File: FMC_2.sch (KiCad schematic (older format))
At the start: 14 parts, among them P2 SAMTEC_ASP-134603-01

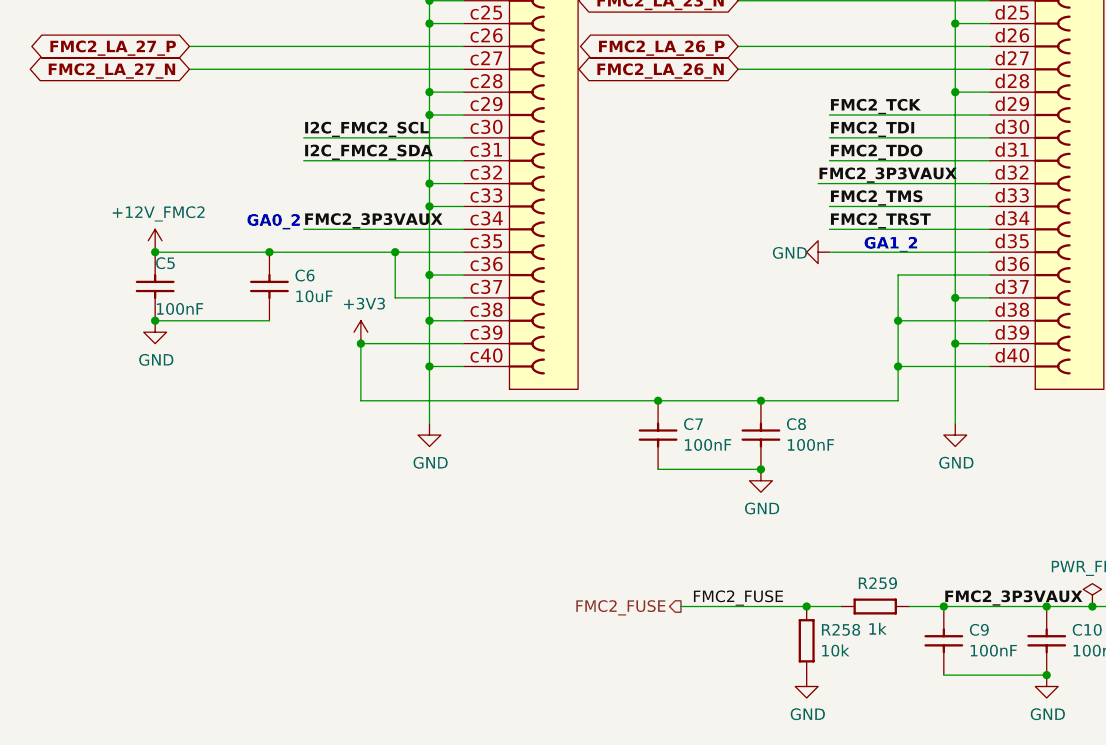
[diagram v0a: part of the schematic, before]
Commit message: Add 300 Ohm series resistors to GA pins
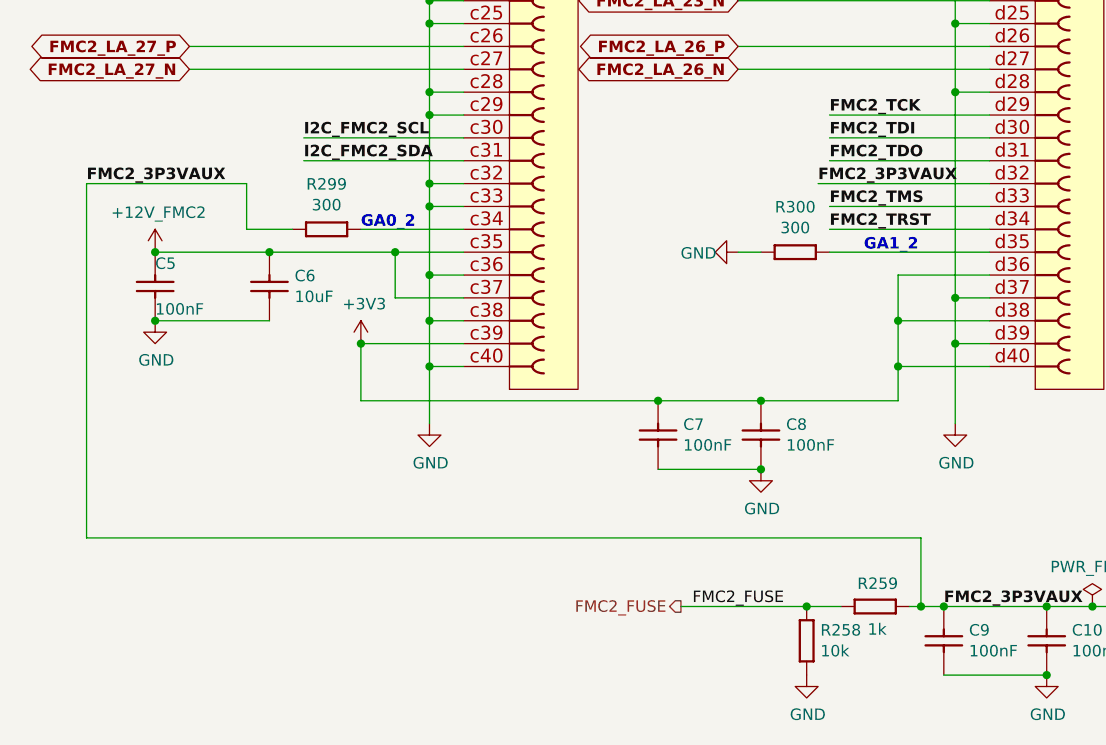
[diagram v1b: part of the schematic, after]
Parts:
- added R299, R300: R0402_300R_1%_0.0625W_100PPM, Resistors SMD:RESC1005X40N, symbol Resistors_SMD:R0402_300R_1%_0.0625W_100PPM
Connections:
- net FMC2_3P3VAUX: now also R299.1; no longer P2.c34
- net GND: now also R300.1; no longer P2.d35
- new net: P2.c34, R299.2
- new net: P2.d35, R300.2
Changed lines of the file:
@@
 Connection ~ 5750 5850
-Wire Wire Line
-	3150 5250 3850 5250
 Wire Wire Line
 	3150 4850 3850 4850
@@
 Wire Wire Line
 	5450 5150 6150 5150
-Wire Wire Line
-	5450 5350 6150 5350
 Text Label 8000 2050 0    50   ~ 10
 FMC2_CLK1_M2C_P
@@
 Wire Wire Line
 	5450 5250 6150 5250
-Text Label 3150 5250 0    50   ~ 10
+Text Label 2200 5050 0    50   ~ 10
 FMC2_3P3VAUX
-Text Notes 2900 5250 0    50   ~ 10
+Text Notes 3400 5250 0    50   ~ 10
 GA0_2
 $Comp
 L power:GND #PWR?
 U 1 1 5D1DC9A3
-P 5450 5350
+P 5050 5350
 AR Path="/5BD32060/5D1DC9A3" Ref="#PWR?"  Part="1"
 AR Path="/5BD31F9A/5D1DC9A3" Ref="#PWR?"  Part="1"
 AR Path="/5BD31F9F/5D1DC9A3" Ref="#PWR0101"  Part="1"
 AR Path="/5D1DC9A3" Ref="#PWR?"  Part="1"
-F 0 "#PWR0101" H 5450 5100 50  0001 C CNN
-F 1 "GND" V 5455 5177 50  0000 C CNN
-F 2 "" H 5450 5350 50  0001 C CNN
-F 3 "" H 5450 5350 50  0001 C CNN
-	1    5450 5350
+F 0 "#PWR0101" H 5050 5100 50  0001 C CNN
+F 1 "GND" V 5055 5177 50  0000 C CNN
+F 2 "" H 5050 5350 50  0001 C CNN
+F 3 "" H 5050 5350 50  0001 C CNN
+	1    5050 5350
 	0    1    1    0
 $EndComp
@@
 $EndComp
 Wire Wire Line
-	5800 6900 5950 6900
+	5800 6900 5850 6900
 Connection ~ 5950 6900
 Wire Wire Line
@@
 Wire Wire Line
 	7150 6900 7300 6900
+$Comp
+L Resistors_SMD:R0402_300R_1%_0.0625W_100PPM R299
+U 1 1 5ED979B2
+P 3100 5250
+F 0 "R299" H 3250 5447 50  0000 C CNN
+F 1 "R0402_300R_1%_0.0625W_100PPM" H 3100 5055 50  0001 L CNN
+F 2 "Resistors SMD:RESC1005X40N" H 3100 4980 50  0001 L CNN
+F 3 " " H 3100 4905 50  0001 L CNN
+F 4 "300" H 3250 5356 50  0000 C CNN "Val"
+F 5 "R0402_300R_1%_0.0625W_100PPM" H 3100 4830 50  0001 L CNN "Part Number"
+F 6 "Resistor - 1%" H 3100 4755 50  0001 L CNN "Library Ref"
+F 7 "SchLib\\Resistors.SchLib" H 3100 4680 50  0001 L CNN "Library Path"
+F 8 "300" H 3100 4605 50  0001 L CNN "Comment"
+F 9 "Standard" H 3100 4530 50  0001 L CNN "Component Kind"
+F 10 "Standard" H 3100 4455 50  0001 L CNN "Component Type"
+F 11 " " H 3100 4380 50  0001 L CNN "PackageDescription"
+F 12 "2" H 3100 4305 50  0001 L CNN "Pin Count"
+F 13 "PcbLib\\Resistors SMD.PcbLib" H 3100 4230 50  0001 L CNN "Footprint Path"
+F 14 "RESC1005X40N" H 3100 4155 50  0001 L CNN "Footprint Ref"
+F 15 "Not Recommended" H 3100 4080 50  0001 L CNN "Status"
+F 16 "0.0625W" H 3100 4005 50  0001 L CNN "Power"
+F 17 "±100ppm/°C" H 3100 3930 50  0001 L CNN "TC"
+F 18 " " H 3100 3855 50  0001 L CNN "Voltage"
+F 19 "±1%" H 3100 3780 50  0001 L CNN "Tolerance"
+F 20 "General Purpose Thick Film Chip Resistor" H 3100 3705 50  0001 L CNN "Part Description"
+F 21 "GENERIC" H 3100 3630 50  0001 L CNN "Manufacturer"
+F 22 "R0402_300R_1%_0.0625W_100PPM" H 3100 3555 50  0001 L CNN "Manufacturer Part Number"
+F 23 "0402" H 3100 3480 50  0001 L CNN "Case"
+F 24 "No" H 3100 3405 50  0001 L CNN "PressFit"
+F 25 "Yes" H 3100 3330 50  0001 L CNN "Mounted"
+F 26 " " H 3100 3255 50  0001 L CNN "Sense Comment"
+F 27 "No" H 3100 3180 50  0001 L CNN "Sense"
+F 28 " " H 3100 3105 50  0001 L CNN "Status Comment"
+F 29 "No" H 3100 3030 50  0001 L CNN "Socket"
+F 30 "Yes" H 3100 2955 50  0001 L CNN "SMD"
+F 31 " " H 3100 2880 50  0001 L CNN "ComponentHeight"
+F 32 "YAGEO PHYCOMP" H 3100 2805 50  0001 L CNN "Manufacturer1 Example"
+F 33 "232270673001L" H 3100 2730 50  0001 L CNN "Manufacturer1 Part Number"
+F 34 "0.4mm" H 3100 2655 50  0001 L CNN "Manufacturer1 ComponentHeight"
+F 35 "CERN DEM JLC" H 3100 2580 50  0001 L CNN "Author"
+F 36 "12/03/07 00:00:00" H 3100 2505 50  0001 L CNN "CreateDate"
+F 37 "10/17/12 00:00:00" H 3100 2430 50  0001 L CNN "LatestRevisionDate"
+F 38 "Resistors SMD" H 3100 2355 50  0001 L CNN "Database Table Name"
+F 39 "Resistors.DbLib" H 3100 2280 50  0001 L CNN "Library Name"
+F 40 "Resistors SMD" H 3100 2205 50  0001 L CNN "Footprint Library"
+F 41 "This work is licensed under the Creative Commons CC-BY-SA 4.0 License. To the extent that circuit schematics that use Licensed Material can be considered to be ‘Adapted Material’, then the copyright holder waives article 3.b of the license with respect to these schematics." H 3100 2130 50  0001 L CNN "License"
+	1    3100 5250
+	1    0    0    -1
+$EndComp
+Wire Wire Line
+	3850 5250 3400 5250
+$Comp
+L Resistors_SMD:R0402_300R_1%_0.0625W_100PPM R300
+U 1 1 5EDF3EEE
+P 5150 5350
+F 0 "R300" H 5300 5547 50  0000 C CNN
+F 1 "R0402_300R_1%_0.0625W_100PPM" H 5150 5155 50  0001 L CNN
+F 2 "Resistors SMD:RESC1005X40N" H 5150 5080 50  0001 L CNN
+F 3 " " H 5150 5005 50  0001 L CNN
+F 4 "300" H 5300 5456 50  0000 C CNN "Val"
+F 5 "R0402_300R_1%_0.0625W_100PPM" H 5150 4930 50  0001 L CNN "Part Number"
+F 6 "Resistor - 1%" H 5150 4855 50  0001 L CNN "Library Ref"
+F 7 "SchLib\\Resistors.SchLib" H 5150 4780 50  0001 L CNN "Library Path"
+F 8 "300" H 5150 4705 50  0001 L CNN "Comment"
+F 9 "Standard" H 5150 4630 50  0001 L CNN "Component Kind"
+F 10 "Standard" H 5150 4555 50  0001 L CNN "Component Type"
+F 11 " " H 5150 4480 50  0001 L CNN "PackageDescription"
+F 12 "2" H 5150 4405 50  0001 L CNN "Pin Count"
+F 13 "PcbLib\\Resistors SMD.PcbLib" H 5150 4330 50  0001 L CNN "Footprint Path"
+F 14 "RESC1005X40N" H 5150 4255 50  0001 L CNN "Footprint Ref"
+F 15 "Not Recommended" H 5150 4180 50  0001 L CNN "Status"
+F 16 "0.0625W" H 5150 4105 50  0001 L CNN "Power"
+F 17 "±100ppm/°C" H 5150 4030 50  0001 L CNN "TC"
+F 18 " " H 5150 3955 50  0001 L CNN "Voltage"
+F 19 "±1%" H 5150 3880 50  0001 L CNN "Tolerance"
+F 20 "General Purpose Thick Film Chip Resistor" H 5150 3805 50  0001 L CNN "Part Description"
+F 21 "GENERIC" H 5150 3730 50  0001 L CNN "Manufacturer"
+F 22 "R0402_300R_1%_0.0625W_100PPM" H 5150 3655 50  0001 L CNN "Manufacturer Part Number"
+F 23 "0402" H 5150 3580 50  0001 L CNN "Case"
+F 24 "No" H 5150 3505 50  0001 L CNN "PressFit"
+F 25 "Yes" H 5150 3430 50  0001 L CNN "Mounted"
+F 26 " " H 5150 3355 50  0001 L CNN "Sense Comment"
+F 27 "No" H 5150 3280 50  0001 L CNN "Sense"
+F 28 " " H 5150 3205 50  0001 L CNN "Status Comment"
+F 29 "No" H 5150 3130 50  0001 L CNN "Socket"
+F 30 "Yes" H 5150 3055 50  0001 L CNN "SMD"
+F 31 " " H 5150 2980 50  0001 L CNN "ComponentHeight"
+F 32 "YAGEO PHYCOMP" H 5150 2905 50  0001 L CNN "Manufacturer1 Example"
+F 33 "232270673001L" H 5150 2830 50  0001 L CNN "Manufacturer1 Part Number"
+F 34 "0.4mm" H 5150 2755 50  0001 L CNN "Manufacturer1 ComponentHeight"
+F 35 "CERN DEM JLC" H 5150 2680 50  0001 L CNN "Author"
+F 36 "12/03/07 00:00:00" H 5150 2605 50  0001 L CNN "CreateDate"
+F 37 "10/17/12 00:00:00" H 5150 2530 50  0001 L CNN "LatestRevisionDate"
+F 38 "Resistors SMD" H 5150 2455 50  0001 L CNN "Database Table Name"
+F 39 "Resistors.DbLib" H 5150 2380 50  0001 L CNN "Library Name"
+F 40 "Resistors SMD" H 5150 2305 50  0001 L CNN "Footprint Library"
+F 41 "This work is licensed under the Creative Commons CC-BY-SA 4.0 License. To the extent that circuit schematics that use Licensed Material can be considered to be ‘Adapted Material’, then the copyright holder waives article 3.b of the license with respect to these schematics." H 5150 2230 50  0001 L CNN "License"
+	1    5150 5350
+	1    0    0    -1
+$EndComp
+Wire Wire Line
+	5150 5350 5050 5350
+Wire Wire Line
+	5450 5350 6150 5350
+Wire Wire Line
+	3100 5250 2900 5250
+Wire Wire Line
+	2900 5250 2900 5050
+Wire Wire Line
+	2900 5050 2200 5050
+Wire Wire Line
+	5850 6900 5850 6600
+Wire Wire Line
+	5850 6600 2200 6600
+Wire Wire Line
+	2200 6600 2200 5050
+Connection ~ 5850 6900
+Wire Wire Line
+	5850 6900 5950 6900
 $EndSCHEMATC

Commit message: change R297 - R300 to 240 Ohm
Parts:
- R299, R300: value R0402_300R_1%_0.0625W_100PPM -> R0402_240R_1%_0.0625W_100PPM; footprint Resistors SMD:RESC1005X40N -> Marble:RESC1005X40N; symbol Resistors_SMD:R0402_300R_1%_0.0625W_100PPM -> Resistors_SMD:R0402_240R_1%_0.0625W_100PPM; Comment 300 -> 240; Manufacturer Part Number R0402_300R_1%_0.0625W_100PPM -> R0402_240R_1%_0.0625W_100PPM; Manufacturer1 Part Number 232270673001L -> 232270672401L; Part Number R0402_300R_1%_0.0625W_100PPM -> R0402_240R_1%_0.0625W_100PPM; Val 300 -> 240
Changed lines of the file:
@@
 	7150 6900 7300 6900
 $Comp
-L Resistors_SMD:R0402_300R_1%_0.0625W_100PPM R299
+L Resistors_SMD:R0402_240R_1%_0.0625W_100PPM R299
 U 1 1 5ED979B2
 P 3100 5250
 F 0 "R299" H 3250 5447 50  0000 C CNN
-F 1 "R0402_300R_1%_0.0625W_100PPM" H 3100 5055 50  0001 L CNN
-F 2 "Resistors SMD:RESC1005X40N" H 3100 4980 50  0001 L CNN
+F 1 "R0402_240R_1%_0.0625W_100PPM" H 3100 5055 50  0001 L CNN
+F 2 "Marble:RESC1005X40N" H 3100 4980 50  0001 L CNN
 F 3 " " H 3100 4905 50  0001 L CNN
-F 4 "300" H 3250 5356 50  0000 C CNN "Val"
-F 5 "R0402_300R_1%_0.0625W_100PPM" H 3100 4830 50  0001 L CNN "Part Number"
+F 4 "240" H 3250 5356 50  0000 C CNN "Val"
+F 5 "R0402_240R_1%_0.0625W_100PPM" H 3100 4830 50  0001 L CNN "Part Number"
 F 6 "Resistor - 1%" H 3100 4755 50  0001 L CNN "Library Ref"
 F 7 "SchLib\\Resistors.SchLib" H 3100 4680 50  0001 L CNN "Library Path"
-F 8 "300" H 3100 4605 50  0001 L CNN "Comment"
+F 8 "240" H 3100 4605 50  0001 L CNN "Comment"
 F 9 "Standard" H 3100 4530 50  0001 L CNN "Component Kind"
 F 10 "Standard" H 3100 4455 50  0001 L CNN "Component Type"
@@
 F 20 "General Purpose Thick Film Chip Resistor" H 3100 3705 50  0001 L CNN "Part Description"
 F 21 "GENERIC" H 3100 3630 50  0001 L CNN "Manufacturer"
-F 22 "R0402_300R_1%_0.0625W_100PPM" H 3100 3555 50  0001 L CNN "Manufacturer Part Number"
+F 22 "R0402_240R_1%_0.0625W_100PPM" H 3100 3555 50  0001 L CNN "Manufacturer Part Number"
 F 23 "0402" H 3100 3480 50  0001 L CNN "Case"
 F 24 "No" H 3100 3405 50  0001 L CNN "PressFit"
@@
 F 31 " " H 3100 2880 50  0001 L CNN "ComponentHeight"
 F 32 "YAGEO PHYCOMP" H 3100 2805 50  0001 L CNN "Manufacturer1 Example"
-F 33 "232270673001L" H 3100 2730 50  0001 L CNN "Manufacturer1 Part Number"
+F 33 "232270672401L" H 3100 2730 50  0001 L CNN "Manufacturer1 Part Number"
 F 34 "0.4mm" H 3100 2655 50  0001 L CNN "Manufacturer1 ComponentHeight"
 F 35 "CERN DEM JLC" H 3100 2580 50  0001 L CNN "Author"
@@
 	3850 5250 3400 5250
 $Comp
-L Resistors_SMD:R0402_300R_1%_0.0625W_100PPM R300
+L Resistors_SMD:R0402_240R_1%_0.0625W_100PPM R300
 U 1 1 5EDF3EEE
 P 5150 5350
 F 0 "R300" H 5300 5547 50  0000 C CNN
-F 1 "R0402_300R_1%_0.0625W_100PPM" H 5150 5155 50  0001 L CNN
-F 2 "Resistors SMD:RESC1005X40N" H 5150 5080 50  0001 L CNN
+F 1 "R0402_240R_1%_0.0625W_100PPM" H 5150 5155 50  0001 L CNN
+F 2 "Marble:RESC1005X40N" H 5150 5080 50  0001 L CNN
 F 3 " " H 5150 5005 50  0001 L CNN
-F 4 "300" H 5300 5456 50  0000 C CNN "Val"
-F 5 "R0402_300R_1%_0.0625W_100PPM" H 5150 4930 50  0001 L CNN "Part Number"
+F 4 "240" H 5300 5456 50  0000 C CNN "Val"
+F 5 "R0402_240R_1%_0.0625W_100PPM" H 5150 4930 50  0001 L CNN "Part Number"
 F 6 "Resistor - 1%" H 5150 4855 50  0001 L CNN "Library Ref"
 F 7 "SchLib\\Resistors.SchLib" H 5150 4780 50  0001 L CNN "Library Path"
-F 8 "300" H 5150 4705 50  0001 L CNN "Comment"
+F 8 "240" H 5150 4705 50  0001 L CNN "Comment"
 F 9 "Standard" H 5150 4630 50  0001 L CNN "Component Kind"
 F 10 "Standard" H 5150 4555 50  0001 L CNN "Component Type"
@@
 F 20 "General Purpose Thick Film Chip Resistor" H 5150 3805 50  0001 L CNN "Part Description"
 F 21 "GENERIC" H 5150 3730 50  0001 L CNN "Manufacturer"
-F 22 "R0402_300R_1%_0.0625W_100PPM" H 5150 3655 50  0001 L CNN "Manufacturer Part Number"
+F 22 "R0402_240R_1%_0.0625W_100PPM" H 5150 3655 50  0001 L CNN "Manufacturer Part Number"
 F 23 "0402" H 5150 3580 50  0001 L CNN "Case"
 F 24 "No" H 5150 3505 50  0001 L CNN "PressFit"
@@
 F 31 " " H 5150 2980 50  0001 L CNN "ComponentHeight"
 F 32 "YAGEO PHYCOMP" H 5150 2905 50  0001 L CNN "Manufacturer1 Example"
-F 33 "232270673001L" H 5150 2830 50  0001 L CNN "Manufacturer1 Part Number"
+F 33 "232270672401L" H 5150 2830 50  0001 L CNN "Manufacturer1 Part Number"
 F 34 "0.4mm" H 5150 2755 50  0001 L CNN "Manufacturer1 ComponentHeight"
 F 35 "CERN DEM JLC" H 5150 2680 50  0001 L CNN "Author"

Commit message: Convert all footprints to use Marble nickname
Includes both .sch and .lib files
Includes both bare footprint names and those with CERN-like nicknames
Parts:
- C10, C11, C7, C8, C9: footprint CAPC0603X33N -> Marble:CAPC0603X33N
- C12, C13: footprint CAPC1608X87N -> Marble:CAPC1608X87N
- C5: footprint CAPC1005X55N -> Marble:CAPC1005X55N
- C6: footprint CAPC3216X140N -> Marble:CAPC3216X140N
- F1: footprint FUSC1608X55N -> Marble:FUSC1608X55N
- P2: footprint SAMTEC_ASP-134603-01 -> Marble:SAMTEC_ASP-134603-01
- R205, R258, R259: footprint RESC1005X40N -> Marble:RESC1005X40N
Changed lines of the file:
@@
 F 0 "R205" V 10754 1560 50  0000 L CNN
 F 1 "R0402_10K_1%_0.0625W_100PPM" H 10650 1290 60  0001 L CNN
-F 2 "RESC1005X40N" H 10650 480 60  0001 L CNN
+F 2 "Marble:RESC1005X40N" H 10650 480 60  0001 L CNN
 F 3 "\\\\cern.ch\\dfs\\Applications\\Altium\\Datasheets\\R0402_Phycomp_RC0402.pdf" H 10650 1110 60  0001 L CNN
 F 4 "10k" V 10845 1560 50  0000 L CNN "~"
@@
 F 0 "C11" V 7504 5910 50  0000 L CNN
 F 1 "CC0201_100NF_6.3V_10%_X5R" H 7400 5540 60  0001 L CNN
-F 2 "CAPC0603X33N" H 7400 4730 60  0001 L CNN
+F 2 "Marble:CAPC0603X33N" H 7400 4730 60  0001 L CNN
 F 3 "\\\\cern.ch\\dfs\\Applications\\Altium\\Datasheets\\CC0201_X5R_AVX.pdf" H 7400 5360 60  0001 L CNN
 F 4 "100nF" V 7595 5910 50  0000 L CNN "~"
@@
 F 0 "C6" V 3104 5460 50  0000 L CNN
 F 1 "CC1206_10UF_16V_10%_X7R" H 3000 5090 60  0001 L CNN
-F 2 "CAPC3216X140N" H 3000 4280 60  0001 L CNN
+F 2 "Marble:CAPC3216X140N" H 3000 4280 60  0001 L CNN
 F 3 "\\\\cern.ch\\dfs\\Applications\\Altium\\Datasheets\\CC1206_X7R_KEMET.pdf" H 3000 4910 60  0001 L CNN
 F 4 "10uF" V 3195 5460 50  0000 L CNN "~"
@@
 F 0 "C7" V 4804 6110 50  0000 L CNN
 F 1 "CC0201_100NF_6.3V_10%_X5R" H 4700 5740 60  0001 L CNN
-F 2 "CAPC0603X33N" H 4700 4930 60  0001 L CNN
+F 2 "Marble:CAPC0603X33N" H 4700 4930 60  0001 L CNN
 F 3 "\\\\cern.ch\\dfs\\Applications\\Altium\\Datasheets\\CC0201_X5R_AVX.pdf" H 4700 5560 60  0001 L CNN
 F 4 "100nF" V 4895 6110 50  0000 L CNN "~"
@@
 F 0 "C13" V 8496 5990 50  0000 R CNN
 F 1 "CC0603_10UF_6.3V_20%_X5R" H 8300 5840 60  0001 L CNN
-F 2 "CAPC1608X87N" H 8300 5030 60  0001 L CNN
+F 2 "Marble:CAPC1608X87N" H 8300 5030 60  0001 L CNN
 F 3 "\\\\cern.ch\\dfs\\Applications\\Altium\\Datasheets\\CC0603_X5R_KEMET.pdf" H 8300 5660 60  0001 L CNN
 F 4 "10uF" V 8405 5990 50  0000 R CNN "~"
@@
 F 0 "C5" V 2550 5350 50  0000 L CNN
 F 1 "CC0402_100NF_16V_10%_X5R" H 2500 5090 60  0001 L CNN
-F 2 "CAPC1005X55N" H 2500 4280 60  0001 L CNN
+F 2 "Marble:CAPC1005X55N" H 2500 4280 60  0001 L CNN
 F 3 "\\\\cern.ch\\dfs\\Applications\\Altium\\Datasheets\\CC0402_X5R_MURATA_GRM.pdf" H 2500 4910 60  0001 L CNN
 F 4 "100nF" V 2750 5350 50  0000 L CNN "~"
@@
 F 0 "F1" H 7000 7097 50  0000 C CNN
 F 1 "FUS0603_BOURNS-SF-0603F050-2" H 6850 6680 60  0001 L CNN
-F 2 "FUSC1608X55N" H 6850 5870 60  0001 L CNN
+F 2 "Marble:FUSC1608X55N" H 6850 5870 60  0001 L CNN
 F 3 "\\\\cern.ch\\dfs\\Applications\\Altium\\Datasheets\\FUSE_BOURNS_SF-0603F.pdf" H 6850 6500 60  0001 L CNN
 F 4 "500mA-50V" H 7000 7006 50  0000 C CNN "~"
@@
 F 0 "P2" H 4377 -200 50  0000 L CNN
 F 1 "SAMTEC_ASP-134603-01" H 4050 -2340 60  0001 L CNN
-F 2 "SAMTEC_ASP-134603-01" H 4050 -3240 60  0001 L CNN
+F 2 "Marble:SAMTEC_ASP-134603-01" H 4050 -3240 60  0001 L CNN
 F 3 "\\\\cern.ch\\dfs\\Applications\\Altium\\Datasheets\\SAMTEC_ASP-134603-01.pdf" H 4050 -2520 60  0001 L CNN
 F 4 "VITA 57" H 4050 -2610 60  0001 L CNN "Pole4"
@@
 F 0 "P2" H 6678 -200 50  0000 L CNN
 F 1 "SAMTEC_ASP-134603-01" H 6350 -2340 60  0001 L CNN
-F 2 "SAMTEC_ASP-134603-01" H 6350 -3240 60  0001 L CNN
+F 2 "Marble:SAMTEC_ASP-134603-01" H 6350 -3240 60  0001 L CNN
 F 3 "\\\\cern.ch\\dfs\\Applications\\Altium\\Datasheets\\SAMTEC_ASP-134603-01.pdf" H 6350 -2520 60  0001 L CNN
 F 4 "VITA 57" H 6350 -2610 60  0001 L CNN "Pole4"
@@
 F 0 "P2" H 9428 -200 50  0000 L CNN
 F 1 "SAMTEC_ASP-134603-01" H 9100 -2340 60  0001 L CNN
-F 2 "SAMTEC_ASP-134603-01" H 9100 -3240 60  0001 L CNN
+F 2 "Marble:SAMTEC_ASP-134603-01" H 9100 -3240 60  0001 L CNN
 F 3 "\\\\cern.ch\\dfs\\Applications\\Altium\\Datasheets\\SAMTEC_ASP-134603-01.pdf" H 9100 -2520 60  0001 L CNN
 F 4 "VITA 57" H 9100 -2610 60  0001 L CNN "Pole4"
@@
 F 0 "P2" H 12078 -200 50  0000 L CNN
 F 1 "SAMTEC_ASP-134603-01" H 11750 -2340 60  0001 L CNN
-F 2 "SAMTEC_ASP-134603-01" H 11750 -3240 60  0001 L CNN
+F 2 "Marble:SAMTEC_ASP-134603-01" H 11750 -3240 60  0001 L CNN
 F 3 "\\\\cern.ch\\dfs\\Applications\\Altium\\Datasheets\\SAMTEC_ASP-134603-01.pdf" H 11750 -2520 60  0001 L CNN
 F 4 "VITA 57" H 11750 -2610 60  0001 L CNN "Pole4"
@@
 F 0 "R258" V 5454 6960 50  0000 L CNN
 F 1 "R0402_10K_1%_0.0625W_100PPM" H 5350 6690 60  0001 L CNN
-F 2 "RESC1005X40N" H 5350 5880 60  0001 L CNN
+F 2 "Marble:RESC1005X40N" H 5350 5880 60  0001 L CNN
 F 3 "\\\\cern.ch\\dfs\\Applications\\Altium\\Datasheets\\R0402_Phycomp_RC0402.pdf" H 5350 6510 60  0001 L CNN
 F 4 "10k" V 5545 6960 50  0000 L CNN "~"
@@
 F 0 "R259" H 5850 6800 50  0000 L CNN
 F 1 "R0402_1K_1%_0.0625W_100PPM" H 5800 6690 60  0001 L CNN
-F 2 "RESC1005X40N" H 5800 5880 60  0001 L CNN
+F 2 "Marble:RESC1005X40N" H 5800 5880 60  0001 L CNN
 F 3 "\\\\cern.ch\\dfs\\Applications\\Altium\\Datasheets\\R0402_Phycomp_RC0402.pdf" H 5800 6510 60  0001 L CNN
 F 4 "1k" H 5900 7000 50  0000 L CNN "~"
@@
 F 0 "C8" V 5254 6110 50  0000 L CNN
 F 1 "CC0201_100NF_6.3V_10%_X5R" H 5150 5740 60  0001 L CNN
-F 2 "CAPC0603X33N" H 5150 4930 60  0001 L CNN
+F 2 "Marble:CAPC0603X33N" H 5150 4930 60  0001 L CNN
 F 3 "\\\\cern.ch\\dfs\\Applications\\Altium\\Datasheets\\CC0201_X5R_AVX.pdf" H 5150 5560 60  0001 L CNN
 F 4 "100nF" V 5345 6110 50  0000 L CNN "~"
@@
 F 0 "C9" V 6054 7010 50  0000 L CNN
 F 1 "CC0201_100NF_6.3V_10%_X5R" H 5950 6640 60  0001 L CNN
-F 2 "CAPC0603X33N" H 5950 5830 60  0001 L CNN
+F 2 "Marble:CAPC0603X33N" H 5950 5830 60  0001 L CNN
 F 3 "\\\\cern.ch\\dfs\\Applications\\Altium\\Datasheets\\CC0201_X5R_AVX.pdf" H 5950 6460 60  0001 L CNN
 F 4 "100nF" V 6145 7010 50  0000 L CNN "~"
@@
 F 0 "C10" V 6504 7010 50  0000 L CNN
 F 1 "CC0201_100NF_6.3V_10%_X5R" H 6400 6640 60  0001 L CNN
-F 2 "CAPC0603X33N" H 6400 5830 60  0001 L CNN
+F 2 "Marble:CAPC0603X33N" H 6400 5830 60  0001 L CNN
 F 3 "\\\\cern.ch\\dfs\\Applications\\Altium\\Datasheets\\CC0201_X5R_AVX.pdf" H 6400 6460 60  0001 L CNN
 F 4 "100nF" V 6595 7010 50  0000 L CNN "~"
@@
 F 0 "C12" V 8096 5990 50  0000 R CNN
 F 1 "CC0603_10UF_6.3V_20%_X5R" H 7900 5840 60  0001 L CNN
-F 2 "CAPC1608X87N" H 7900 5030 60  0001 L CNN
+F 2 "Marble:CAPC1608X87N" H 7900 5030 60  0001 L CNN
 F 3 "\\\\cern.ch\\dfs\\Applications\\Altium\\Datasheets\\CC0603_X5R_KEMET.pdf" H 7900 5660 60  0001 L CNN
 F 4 "10uF" V 8005 5990 50  0000 R CNN "~"
